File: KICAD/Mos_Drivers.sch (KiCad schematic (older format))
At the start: 0 parts

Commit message: labels dans les blocks
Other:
- note added: "Entrées"
- note added: "Sorties"
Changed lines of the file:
@@
 $Descr A4 11693 8268
 encoding utf-8
-Sheet 8 15
+Sheet 15 15
 Title "SESAME"
 Date ""
@@
 Comment4 ""
 $EndDescr
+Text HLabel 6300 3200 2    50   Output ~ 0
+VG_LP
+Text HLabel 6300 3300 2    50   Output ~ 0
+VG_LS
+Text HLabel 6300 3400 2    50   Output ~ 0
+VG_RP
+Text HLabel 6300 3500 2    50   Output ~ 0
+VG_RS
+Text HLabel 5650 3200 0    50   Input ~ 0
+Driver_LS
+Text HLabel 5650 3100 0    50   Input ~ 0
+Driver_LP
+Text HLabel 5650 3300 0    50   Input ~ 0
+Driver_RP
+Text HLabel 5650 3400 0    50   Input ~ 0
+Driver_RS
+Text HLabel 5650 3500 0    50   Input ~ 0
+Enable
+Text Notes 5300 3650 0    50   ~ 0
+Entrées
+Text Notes 6300 3650 0    50   ~ 0
+Sorties
+Wire Notes Line
+	6250 3100 6650 3100
+Wire Notes Line
+	6650 3100 6650 3700
+Wire Notes Line
+	6650 3700 6250 3700
+Wire Notes Line
+	6250 3700 6250 3100
+Wire Notes Line
+	5700 3000 5200 3000
+Wire Notes Line
+	5200 3000 5200 3700
+Wire Notes Line
+	5200 3700 5700 3700
+Wire Notes Line
+	5700 3700 5700 3000
 $EndSCHEMATC

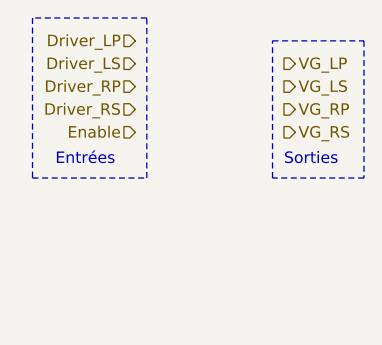
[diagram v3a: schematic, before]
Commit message: minors edits + 7v rail
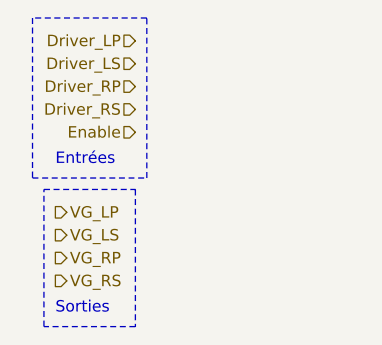
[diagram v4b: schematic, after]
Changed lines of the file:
@@
 Comment4 ""
 $EndDescr
-Text HLabel 6300 3200 2    50   Output ~ 0
+Text HLabel 5300 3850 2    50   Output ~ 0
 VG_LP
-Text HLabel 6300 3300 2    50   Output ~ 0
+Text HLabel 5300 3950 2    50   Output ~ 0
 VG_LS
-Text HLabel 6300 3400 2    50   Output ~ 0
+Text HLabel 5300 4050 2    50   Output ~ 0
 VG_RP
-Text HLabel 6300 3500 2    50   Output ~ 0
+Text HLabel 5300 4150 2    50   Output ~ 0
 VG_RS
 Text HLabel 5650 3200 0    50   Input ~ 0
@@
 Text Notes 5300 3650 0    50   ~ 0
 Entrées
-Text Notes 6300 3650 0    50   ~ 0
+Text Notes 5300 4300 0    50   ~ 0
 Sorties
 Wire Notes Line
-	6250 3100 6650 3100
+	5250 3750 5650 3750
 Wire Notes Line
-	6650 3100 6650 3700
+	5650 3750 5650 4350
 Wire Notes Line
-	6650 3700 6250 3700
+	5650 4350 5250 4350
 Wire Notes Line
-	6250 3700 6250 3100
+	5250 4350 5250 3750
 Wire Notes Line
 	5700 3000 5200 3000

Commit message: ebauche driver mos
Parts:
- added C?: 100n, symbol Device:C
- added C?: C, symbol Device:C
- added D? (x2): D_Schottky, symbol Device:D_Schottky
- added D? (x2): D, symbol Device:D
- added R? (x4): R, symbol Device:R
- added U?: UCC27714D, Package_SO:SOIC-14_3.9x8.7mm_P1.27mm, symbol Driver_FET:UCC27714D
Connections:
- net Driver_LP: now also U?.2 (LI)
- net Driver_LS: now also U?.1 (HI)
- net Enable: now also U?.4 (EN/NC)
- net VG_LP: now also D?.2 (A), R?.1
- net VG_LS: now also D?.2 (A), R?.1
- new net: D?.1 (K), R?.2, R?.2, U?.12 (HO)
- new net: C?.1, U?.13 (HB)
- new net: D?.1 (K), R?.2, R?.2, U?.6 (LO)
- new net: D?.1 (K), R?.1 (x2)
- new net +7V: C?.1, U?.7 (VDD)
- new net GND: C?.2, D?.2 (A), U?.3 (VSS)
- new net VS_L: C?.2, D?.2 (A), U?.11 (HS)
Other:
- note added: "https://www.microchip.com/en-us/parametric-search.html/385 MCP14628"
- note removed: "Entrées"

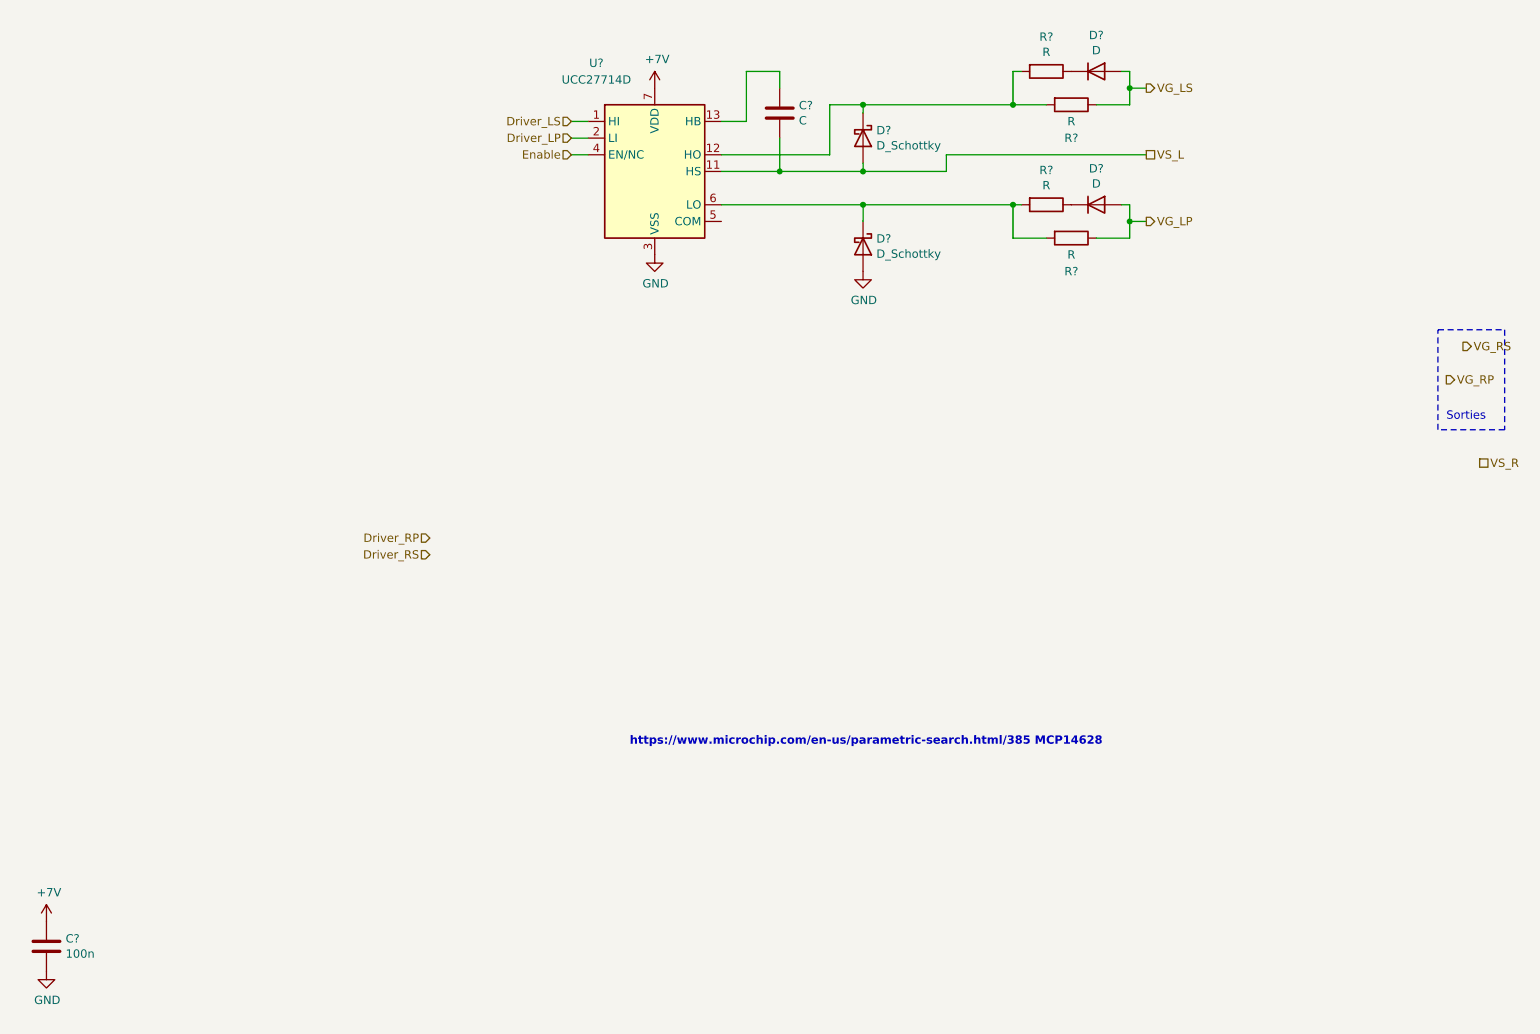
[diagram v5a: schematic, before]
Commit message: added draft pwm gen & pid
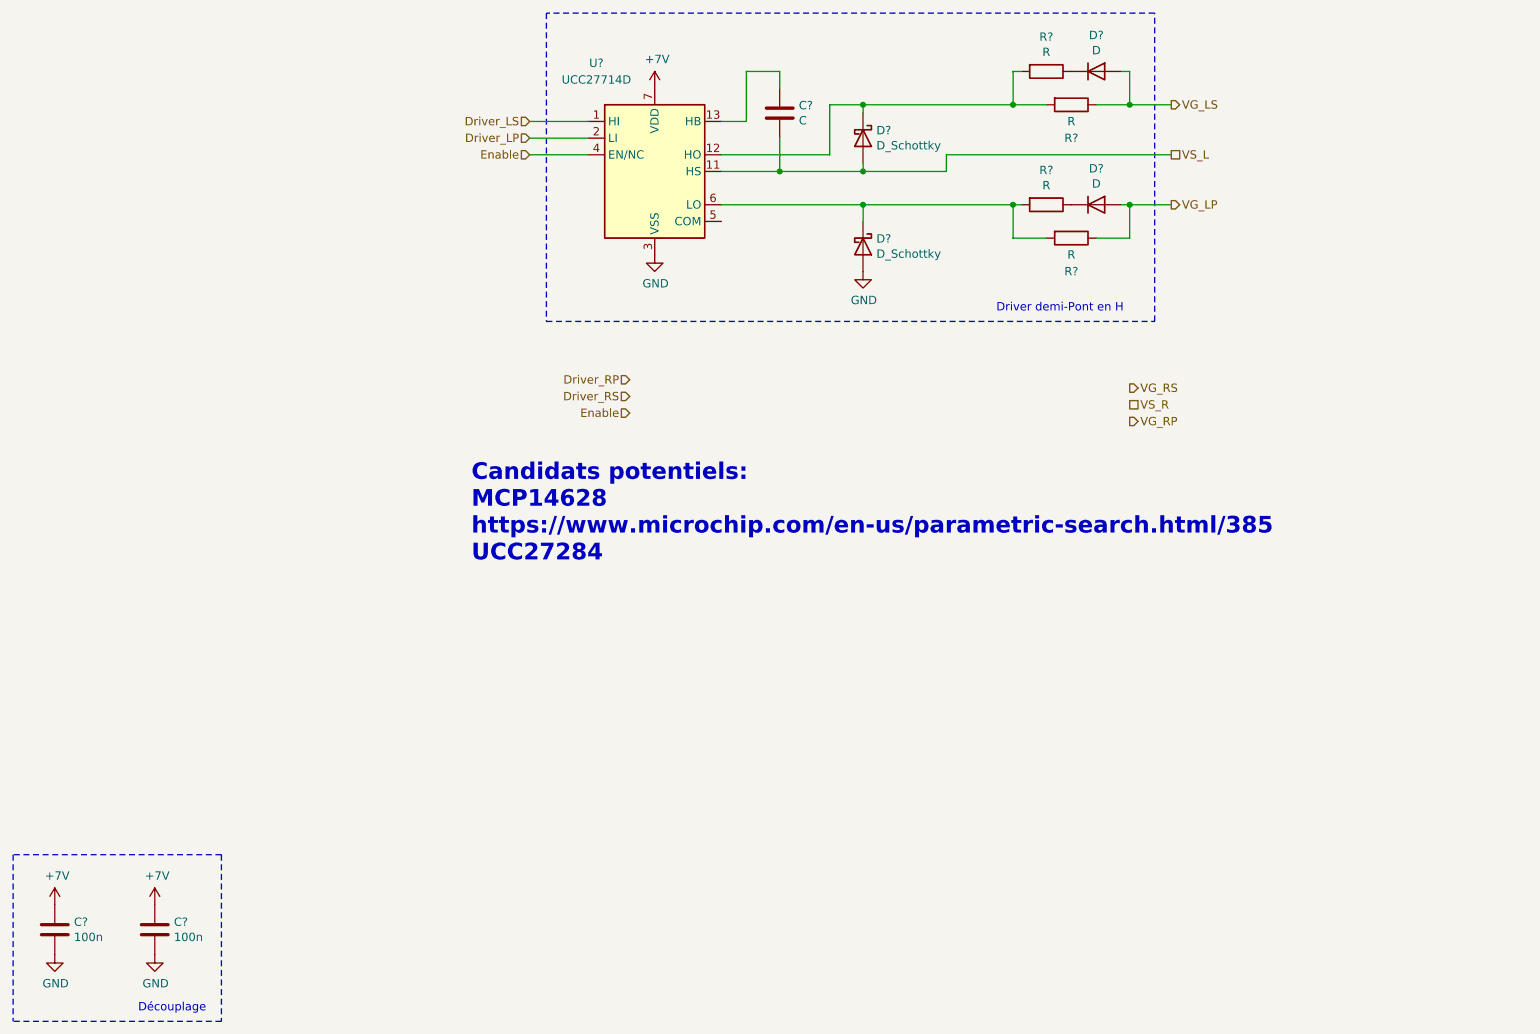
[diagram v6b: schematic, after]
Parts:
- added C?: 100n, symbol Device:C
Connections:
- net +7V: now also C?.1
- net GND: now also C?.2
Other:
- note added: "Candidats potentiels:\nMCP14628\nhttps://www.microchip.com/en-us/parametric-search.html/385\nUCC27284"
- note added: "Driver demi-Pont en H"
- note added: "Découplage"
- note removed: "Sorties"
- note removed: "https://www.microchip.com/en-us/parametric-search.html/385 MCP14628"
- moved on the sheet: C?
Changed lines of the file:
@@
 Comment4 ""
 $EndDescr
-Text HLabel 7400 2850 2    50   Output ~ 0
+Text HLabel 7550 2750 2    50   Output ~ 0
 VG_LP
-Text HLabel 9200 3800 2    50   Output ~ 0
+Text HLabel 7300 4050 2    50   Output ~ 0
 VG_RP
-Text HLabel 9300 3600 2    50   Output ~ 0
+Text HLabel 7300 3850 2    50   Output ~ 0
 VG_RS
-Text HLabel 3950 2250 0    50   Input ~ 0
+Text HLabel 3700 2250 0    50   Input ~ 0
 Driver_LS
-Text HLabel 3950 2350 0    50   Input ~ 0
+Text HLabel 3700 2350 0    50   Input ~ 0
 Driver_LP
-Text HLabel 3100 4750 0    50   Input ~ 0
+Text HLabel 4300 3800 0    50   Input ~ 0
 Driver_RP
-Text HLabel 3100 4850 0    50   Input ~ 0
+Text HLabel 4300 3900 0    50   Input ~ 0
 Driver_RS
-Text HLabel 3950 2450 0    50   Input ~ 0
+Text HLabel 3700 2450 0    50   Input ~ 0
 Enable
-Text Notes 9200 4050 0    50   ~ 0
-Sorties
-Wire Notes Line
-	9150 3500 9550 3500
-Wire Notes Line
-	9550 3500 9550 4100
-Wire Notes Line
-	9550 4100 9150 4100
-Wire Notes Line
-	9150 4100 9150 3500
-Text Notes 4300 6000 0    50   ~ 10
-https://www.microchip.com/en-us/parametric-search.html/385 MCP14628
+Text Notes 3350 4900 0    100  ~ 20
+Candidats potentiels:\nMCP14628\nhttps://www.microchip.com/en-us/parametric-search.html/385\nUCC27284
 $Comp
 L Driver_FET:UCC27714D U?
@@
 L Device:C C?
 U 1 1 612BC387
-P 800 7200
-F 0 "C?" H 915 7246 50  0000 L CNN
-F 1 "100n" H 915 7155 50  0000 L CNN
-F 2 "" H 838 7050 50  0001 C CNN
-F 3 "~" H 800 7200 50  0001 C CNN
-	1    800  7200
+P 850 7100
+F 0 "C?" H 965 7146 50  0000 L CNN
+F 1 "100n" H 965 7055 50  0000 L CNN
+F 2 "" H 888 6950 50  0001 C CNN
+F 3 "~" H 850 7100 50  0001 C CNN
+	1    850  7100
 	1    0    0    -1
 $EndComp
@@
 L Sesame:+7V #PWR?
 U 1 1 612BCBD1
-P 800 7050
-F 0 "#PWR?" H 800 6900 50  0001 C CNN
-F 1 "+7V" H 815 7223 50  0000 C CNN
-F 2 "" H 800 7050 50  0001 C CNN
-F 3 "" H 800 7050 50  0001 C CNN
-	1    800  7050
+P 850 6950
+F 0 "#PWR?" H 850 6800 50  0001 C CNN
+F 1 "+7V" H 865 7123 50  0000 C CNN
+F 2 "" H 850 6950 50  0001 C CNN
+F 3 "" H 850 6950 50  0001 C CNN
+	1    850  6950
 	1    0    0    -1
 $EndComp
@@
 L power:GND #PWR?
 U 1 1 612BD1C9
-P 800 7350
-F 0 "#PWR?" H 800 7100 50  0001 C CNN
-F 1 "GND" H 805 7177 50  0000 C CNN
-F 2 "" H 800 7350 50  0001 C CNN
-F 3 "" H 800 7350 50  0001 C CNN
-	1    800  7350
+P 850 7250
+F 0 "#PWR?" H 850 7000 50  0001 C CNN
+F 1 "GND" H 855 7077 50  0000 C CNN
+F 2 "" H 850 7250 50  0001 C CNN
+F 3 "" H 850 7250 50  0001 C CNN
+	1    850  7250
 	1    0    0    -1
 $EndComp
@@
 $EndComp
 Wire Wire Line
-	3950 2350 4050 2350
-Wire Wire Line
-	4050 2250 3950 2250
-Wire Wire Line
-	3950 2450 4050 2450
+	3700 2350 4050 2350
+Wire Wire Line
+	4050 2250 3700 2250
+Wire Wire Line
+	3700 2450 4050 2450
 $Comp
 L Device:D_Schottky D?
@@
 Connection ~ 5700 2750
 Connection ~ 5700 2150
-Text HLabel 7400 2050 2    50   Output ~ 0
+Text HLabel 7550 2150 2    50   Output ~ 0
 VG_LS
-Text HLabel 7400 2450 2    50   UnSpc ~ 0
+Text HLabel 7550 2450 2    50   UnSpc ~ 0
 VS_L
 Connection ~ 5700 2550
-Text HLabel 9400 4300 2    50   UnSpc ~ 0
+Text HLabel 7300 3950 2    50   UnSpc ~ 0
 VS_R
 $Comp
@@
 	7100 2150 7300 2150
 Wire Wire Line
-	7300 2150 7300 2050
-Wire Wire Line
 	7300 1950 7250 1950
 Wire Wire Line
@@
 	7100 2950 7300 2950
 Wire Wire Line
-	7300 2950 7300 2850
-Wire Wire Line
 	7300 2750 7250 2750
 Wire Wire Line
@@
 	6600 2950 6800 2950
 Wire Wire Line
-	7400 2050 7300 2050
-Connection ~ 7300 2050
-Wire Wire Line
-	7300 2050 7300 1950
-Wire Wire Line
-	7400 2850 7300 2850
-Connection ~ 7300 2850
-Wire Wire Line
-	7300 2850 7300 2750
+	7550 2750 7300 2750
 Wire Wire Line
 	5700 2750 6600 2750
@@
 	6200 2450 6200 2550
 Wire Wire Line
-	6200 2450 7400 2450
+	6200 2450 7550 2450
+Text HLabel 4300 4000 0    50   Input ~ 0
+Enable
+Wire Notes Line
+	3800 1600 3800 3450
+Wire Notes Line
+	3800 3450 7450 3450
+Wire Notes Line
+	7450 3450 7450 1600
+Wire Notes Line
+	7450 1600 3800 1600
+Wire Wire Line
+	7300 1950 7300 2150
+Connection ~ 7300 2750
+Wire Wire Line
+	7300 2750 7300 2950
+Wire Wire Line
+	7550 2150 7300 2150
+Connection ~ 7300 2150
+Text Notes 6500 3400 0    50   ~ 0
+Driver demi-Pont en H
+$Comp
+L Device:C C?
+U 1 1 613B24FD
+P 1450 7100
+F 0 "C?" H 1565 7146 50  0000 L CNN
+F 1 "100n" H 1565 7055 50  0000 L CNN
+F 2 "" H 1488 6950 50  0001 C CNN
+F 3 "~" H 1450 7100 50  0001 C CNN
+	1    1450 7100
+	1    0    0    -1
+$EndComp
+$Comp
+L Sesame:+7V #PWR?
+U 1 1 613B2503
+P 1450 6950
+F 0 "#PWR?" H 1450 6800 50  0001 C CNN
+F 1 "+7V" H 1465 7123 50  0000 C CNN
+F 2 "" H 1450 6950 50  0001 C CNN
+F 3 "" H 1450 6950 50  0001 C CNN
+	1    1450 6950
+	1    0    0    -1
+$EndComp
+$Comp
+L power:GND #PWR?
+U 1 1 613B2509
+P 1450 7250
+F 0 "#PWR?" H 1450 7000 50  0001 C CNN
+F 1 "GND" H 1455 7077 50  0000 C CNN
+F 2 "" H 1450 7250 50  0001 C CNN
+F 3 "" H 1450 7250 50  0001 C CNN
+	1    1450 7250
+	1    0    0    -1
+$EndComp
+Wire Notes Line
+	1850 6650 600  6650
+Text Notes 1350 7600 0    50   ~ 0
+Découplage
+Wire Notes Line
+	1850 7650 600  7650
+Wire Notes Line
+	1850 6650 1850 7650
+Wire Notes Line
+	600  6650 600  7650
 $EndSCHEMATC

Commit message: a ton of new stuff. V0.8
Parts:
- added C?: 100n, symbol Device:C
- added R?: 1k, symbol Device:R
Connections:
- net Enable: now also R?.2; no longer U?.4 (EN/NC)
- net GND: now also C?.2
- net +7V renamed VCC
- new net Enable_Softstart: C?.1, R?.1, U?.4 (EN/NC)
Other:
- note added: "Candidats potentiels:\nMCP14628\nhttps://www.microchip.com/en-us/parametric-search.html/385\n-> UCC27284 (pas sourcable)\nBesoin: \nHalfBridge driver\nPWM & ~PWM~\nRapidité < 100ns\nAlim 7v\n(Pas cher)\nChez RS\nCourant de grille vers 2.5 - 3 A\nEnable\nMode DC !!"
- note added: "au plus vite (juste apres le triangle)\nenv 0.1ms"
- note added: "choisir capacité + empreinte"
- note removed: "Candidats potentiels:\nMCP14628\nhttps://www.microchip.com/en-us/parametric-search.html/385\nUCC27284"
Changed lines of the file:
@@
 $Descr A4 11693 8268
 encoding utf-8
-Sheet 15 15
+Sheet 15 16
 Title "SESAME"
 Date ""
@@
 Text HLabel 4300 3900 0    50   Input ~ 0
 Driver_RS
-Text HLabel 3700 2450 0    50   Input ~ 0
+Text HLabel 1600 2450 0    50   Input ~ 0
 Enable
-Text Notes 3350 4900 0    100  ~ 20
-Candidats potentiels:\nMCP14628\nhttps://www.microchip.com/en-us/parametric-search.html/385\nUCC27284
+Text Notes 3050 6550 0    100  ~ 20
+Candidats potentiels:\nMCP14628\nhttps://www.microchip.com/en-us/parametric-search.html/385\n-> UCC27284 (pas sourcable)\nBesoin: \nHalfBridge driver\nPWM & ~PWM~\nRapidité < 100ns\nAlim 7v\n(Pas cher)\nChez RS\nCourant de grille vers 2.5 - 3 A\nEnable\nMode DC !!
 $Comp
 L Driver_FET:UCC27714D U?
@@
 $EndComp
 $Comp
-L Sesame:+7V #PWR?
-U 1 1 612BB26E
-P 4450 2050
-F 0 "#PWR?" H 4450 1900 50  0001 C CNN
-F 1 "+7V" H 4465 2223 50  0000 C CNN
-F 2 "" H 4450 2050 50  0001 C CNN
-F 3 "" H 4450 2050 50  0001 C CNN
-	1    4450 2050
-	1    0    0    -1
-$EndComp
-$Comp
 L Device:C C?
 U 1 1 612BC387
@@
 $EndComp
 $Comp
-L Sesame:+7V #PWR?
-U 1 1 612BCBD1
-P 850 6950
-F 0 "#PWR?" H 850 6800 50  0001 C CNN
-F 1 "+7V" H 865 7123 50  0000 C CNN
-F 2 "" H 850 6950 50  0001 C CNN
-F 3 "" H 850 6950 50  0001 C CNN
-	1    850  6950
-	1    0    0    -1
-$EndComp
-$Comp
-L power:GND #PWR?
+L power:GND #PWR0179
 U 1 1 612BD1C9
 P 850 7250
-F 0 "#PWR?" H 850 7000 50  0001 C CNN
+F 0 "#PWR0179" H 850 7000 50  0001 C CNN
 F 1 "GND" H 855 7077 50  0000 C CNN
 F 2 "" H 850 7250 50  0001 C CNN
@@
 $EndComp
 $Comp
-L power:GND #PWR?
+L power:GND #PWR0180
 U 1 1 612BD72C
 P 4450 3050
-F 0 "#PWR?" H 4450 2800 50  0001 C CNN
+F 0 "#PWR0180" H 4450 2800 50  0001 C CNN
 F 1 "GND" H 4455 2877 50  0000 C CNN
 F 2 "" H 4450 3050 50  0001 C CNN
@@
 Wire Wire Line
 	4050 2250 3700 2250
-Wire Wire Line
-	3700 2450 4050 2450
 $Comp
 L Device:D_Schottky D?
@@
 	5700 2750 5700 2850
 $Comp
-L power:GND #PWR?
+L power:GND #PWR0181
 U 1 1 612C2683
 P 5700 3150
-F 0 "#PWR?" H 5700 2900 50  0001 C CNN
+F 0 "#PWR0181" H 5700 2900 50  0001 C CNN
 F 1 "GND" H 5705 2977 50  0000 C CNN
 F 2 "" H 5700 3150 50  0001 C CNN
@@
 Wire Wire Line
 	6200 2450 7550 2450
-Text HLabel 4300 4000 0    50   Input ~ 0
-Enable
 Wire Notes Line
 	3800 1600 3800 3450
@@
 $EndComp
 $Comp
-L Sesame:+7V #PWR?
-U 1 1 613B2503
-P 1450 6950
-F 0 "#PWR?" H 1450 6800 50  0001 C CNN
-F 1 "+7V" H 1465 7123 50  0000 C CNN
-F 2 "" H 1450 6950 50  0001 C CNN
-F 3 "" H 1450 6950 50  0001 C CNN
-	1    1450 6950
-	1    0    0    -1
-$EndComp
-$Comp
-L power:GND #PWR?
+L power:GND #PWR0182
 U 1 1 613B2509
 P 1450 7250
-F 0 "#PWR?" H 1450 7000 50  0001 C CNN
+F 0 "#PWR0182" H 1450 7000 50  0001 C CNN
 F 1 "GND" H 1455 7077 50  0000 C CNN
 F 2 "" H 1450 7250 50  0001 C CNN
@@
 Wire Notes Line
 	600  6650 600  7650
+Text Notes 4800 1900 0    50   ~ 0
+choisir capacité + empreinte
+Wire Wire Line
+	2050 2950 2050 3250
+$Comp
+L power:GND #PWR?
+U 1 1 61371978
+P 2050 3250
+AR Path="/60F2F8DD/61371978" Ref="#PWR?"  Part="1"
+AR Path="/60F19D6C/61371978" Ref="#PWR0183"  Part="1"
+F 0 "#PWR0183" H 2050 3000 50  0001 C CNN
+F 1 "GND" H 2055 3077 50  0000 C CNN
+F 2 "" H 2050 3250 50  0001 C CNN
+F 3 "" H 2050 3250 50  0001 C CNN
+	1    2050 3250
+	1    0    0    -1
+$EndComp
+Wire Wire Line
+	2050 2450 2050 2650
+Wire Wire Line
+	1900 2450 2050 2450
+$Comp
+L Device:C C?
+U 1 1 61371980
+P 2050 2800
+AR Path="/60F2F8DD/61371980" Ref="C?"  Part="1"
+AR Path="/60F19D6C/61371980" Ref="C?"  Part="1"
+F 0 "C?" H 2165 2846 50  0000 L CNN
+F 1 "100n" H 2165 2755 50  0000 L CNN
+F 2 "" H 2088 2650 50  0001 C CNN
+F 3 "~" H 2050 2800 50  0001 C CNN
+	1    2050 2800
+	1    0    0    -1
+$EndComp
+$Comp
+L Device:R R?
+U 1 1 61371986
+P 1750 2450
+AR Path="/60F2F8DD/61371986" Ref="R?"  Part="1"
+AR Path="/60F19D6C/61371986" Ref="R?"  Part="1"
+F 0 "R?" V 1543 2450 50  0000 C CNN
+F 1 "1k" V 1634 2450 50  0000 C CNN
+F 2 "" V 1680 2450 50  0001 C CNN
+F 3 "~" H 1750 2450 50  0001 C CNN
+	1    1750 2450
+	0    1    1    0
+$EndComp
+Connection ~ 2050 2450
+Text Label 2700 2450 2    50   ~ 0
+Enable_Softstart
+Text Notes 2150 3050 0    50   ~ 0
+au plus vite (juste apres le triangle)\nenv 0.1ms
+$Comp
+L power:VCC #PWR0184
+U 1 1 6157B763
+P 4450 2050
+F 0 "#PWR0184" H 4450 1900 50  0001 C CNN
+F 1 "VCC" H 4465 2223 50  0000 C CNN
+F 2 "" H 4450 2050 50  0001 C CNN
+F 3 "" H 4450 2050 50  0001 C CNN
+	1    4450 2050
+	1    0    0    -1
+$EndComp
+Wire Wire Line
+	2050 2450 4050 2450
+$Comp
+L power:VCC #PWR0185
+U 1 1 6157FC90
+P 850 6950
+F 0 "#PWR0185" H 850 6800 50  0001 C CNN
+F 1 "VCC" H 865 7123 50  0000 C CNN
+F 2 "" H 850 6950 50  0001 C CNN
+F 3 "" H 850 6950 50  0001 C CNN
+	1    850  6950
+	1    0    0    -1
+$EndComp
+$Comp
+L power:VCC #PWR0186
+U 1 1 61580987
+P 1450 6950
+F 0 "#PWR0186" H 1450 6800 50  0001 C CNN
+F 1 "VCC" H 1465 7123 50  0000 C CNN
+F 2 "" H 1450 6950 50  0001 C CNN
+F 3 "" H 1450 6950 50  0001 C CNN
+	1    1450 6950
+	1    0    0    -1
+$EndComp
 $EndSCHEMATC
